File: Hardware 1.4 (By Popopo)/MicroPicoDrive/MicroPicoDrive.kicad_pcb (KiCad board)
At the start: 2 copper layers, 63.1 x 55.9 mm, 31 parts, among them IC1 SN74LVC1T45DBVR, IC2 SN74LVC1T45DBVR, IC3 TXU0304QPWRQ1, J1 Conn_02x16, J2 QL_CONN, Q1 Q_NPN_BEC, U1 LM7805_TO220, U2 Pico

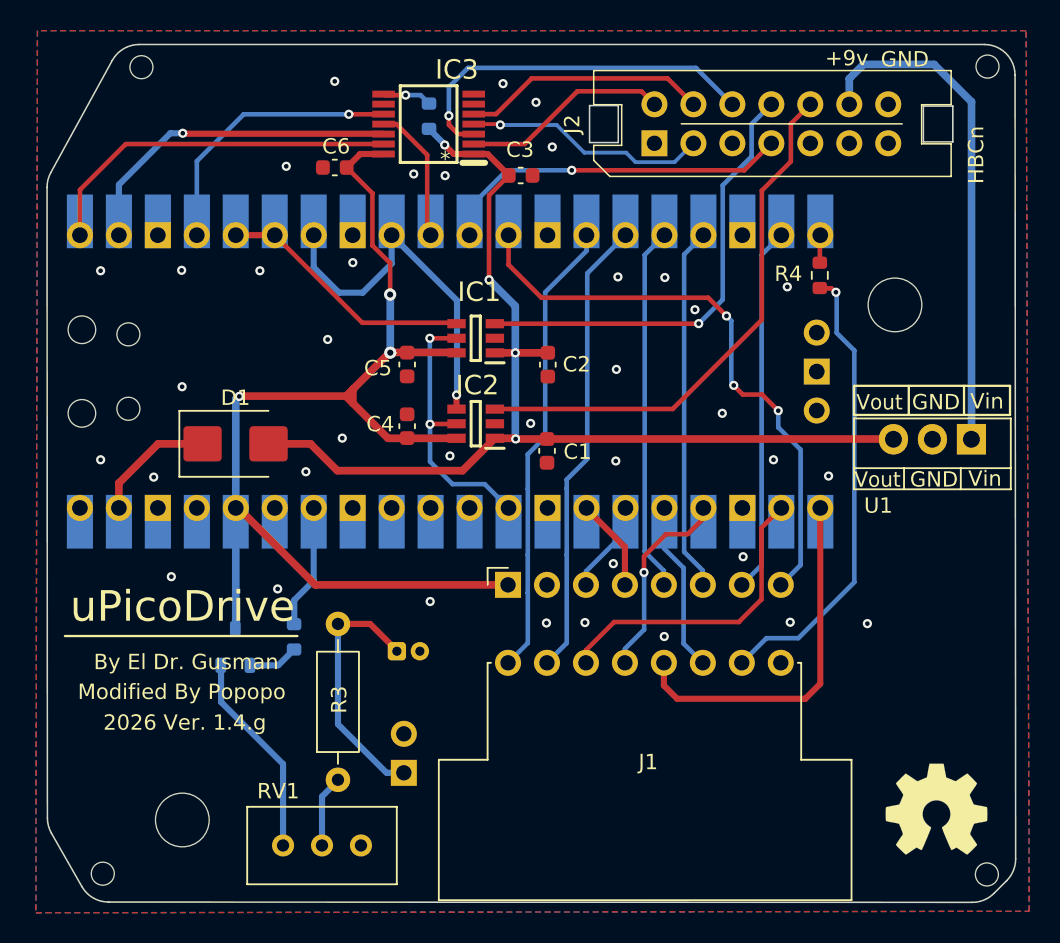
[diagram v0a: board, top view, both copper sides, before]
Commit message: removing rivets
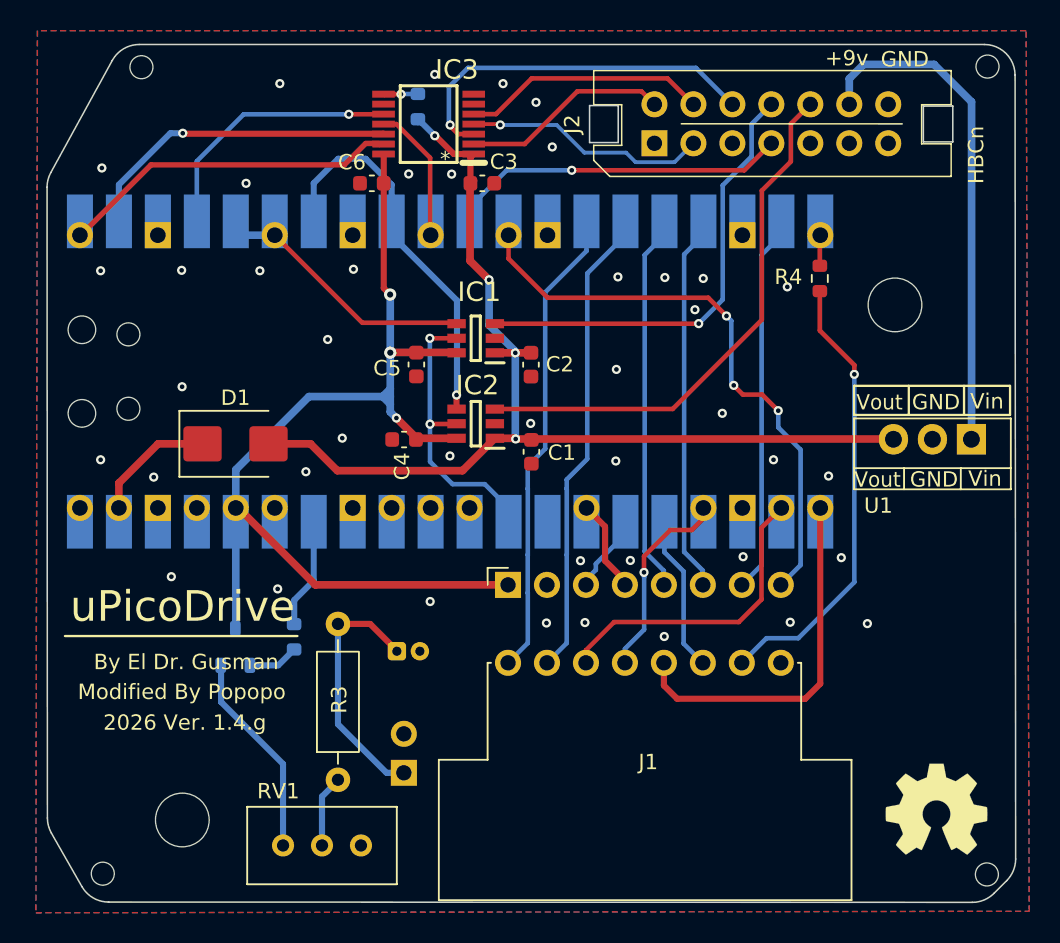
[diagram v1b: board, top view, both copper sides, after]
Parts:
- moved C6 2.63 mm to (138.0, 84.2)
- moved C3 2.55 mm to (145.2, 84.2)
- moved C2 1.10 mm to (148.4, 96.0)
- moved C1 1.02 mm to (148.4, 101.7)
- moved R1 0.96 mm to (141.0, 79.2)
- moved C4 0.89 mm to (140.1, 100.9), turned to 180 degrees
- moved C5 0.60 mm to (140.9, 96.0)
- moved R4 0.20 mm to (167.2, 90.4)
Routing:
- net +3V3: track 75.9 -> 70.0 mm
- net /PICO_HEAD2: track 23.6 -> 26.2 mm
- net /PICO_CS_IN: track 24.0 -> 22.1 mm
- net +5V: track 70.7 -> 69.6 mm
- net Net-(IC3-OE): track 3.22 -> 2.53 mm
- net /UI_DETECT: track 30.1 -> 29.4 mm
- net GND: vias 38 -> 43

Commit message: finished driver PCB rev h
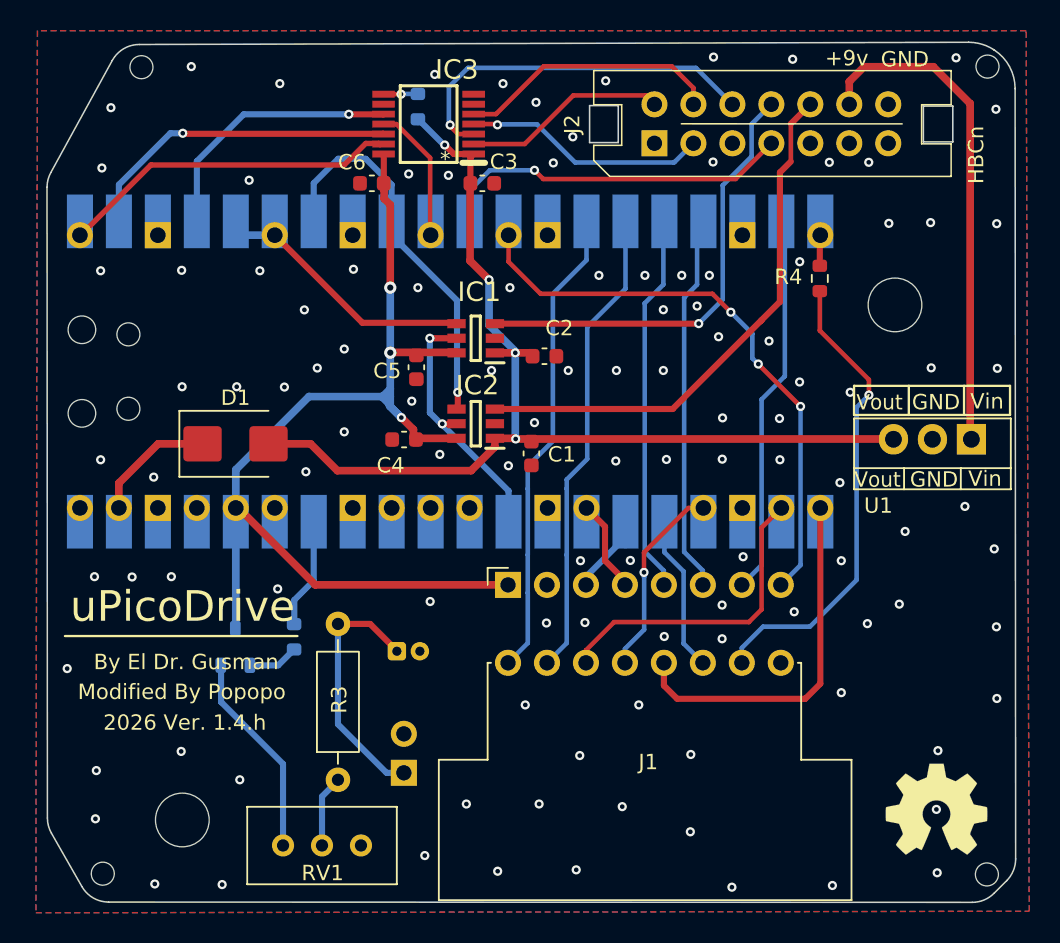
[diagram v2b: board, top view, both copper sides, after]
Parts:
- moved C2 1.04 mm to (149.2, 95.5), turned to 0 degrees
- moved C5 0.18 mm to (140.9, 96.2)
- moved C1 0.11 mm to (148.4, 101.8)
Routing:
- net /UI_SCR_SDA: track 6.08 -> 8.52 mm
- net /HEAD_DIR: track 17.9 -> 15.9 mm
- net /UI_DETECT: track 29.4 -> 30.8 mm
- net +3V3: track 70.0 -> 71.3 mm
- net /QL_CS_OUT: track 16.0 -> 17.3 mm
- net /QL2PICO_ERASE: track 23.2 -> 24.3 mm
- net GND: vias 43 -> 113
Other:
- board size 63.1 x 55.9 mm -> 63.1 x 56.1 mm
- board text added: "2026 Ver. 1.4.h"
- board text removed: "2026 Ver. 1.4.g"

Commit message: last changes
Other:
- board text added: "WayWayWay"
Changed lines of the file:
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@@
+		)
+	)
+	(gr_text "WayWayWay"
+		(at 132.55 99.95 0)
+		(layer "B.SilkS")
+		(effects
+			(font
+				(size 1 1)
+				(thickness 0.15)
+			)
+			(justify left bottom mirror)
 		)
 	)
